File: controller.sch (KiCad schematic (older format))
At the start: 29 parts

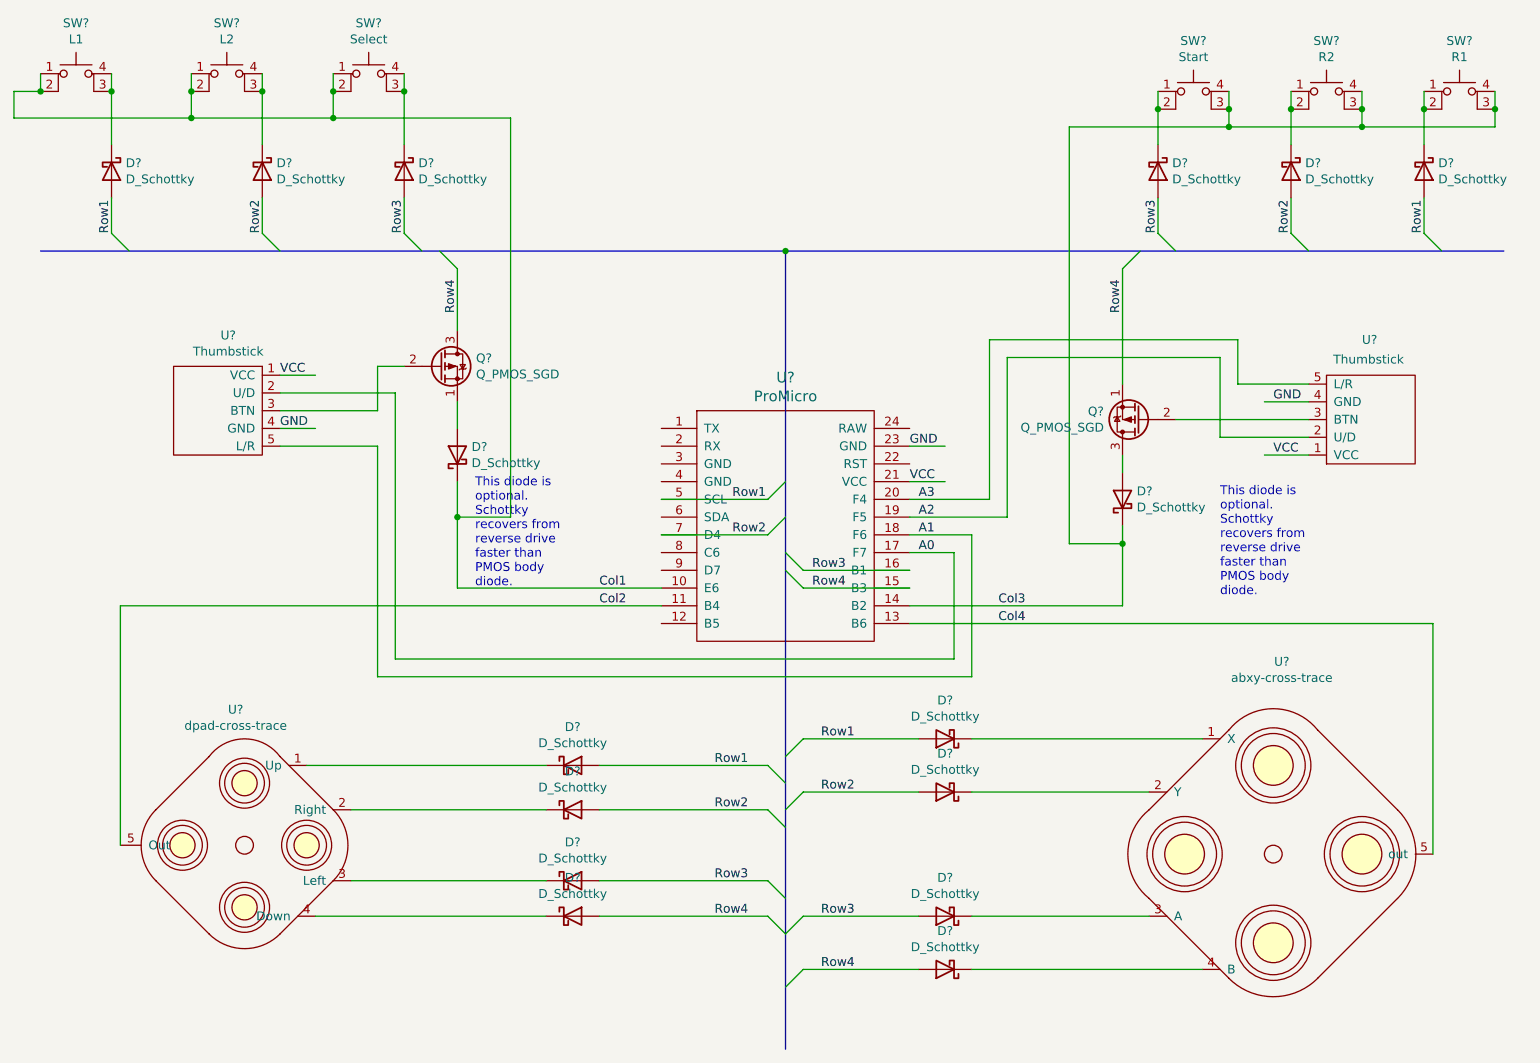
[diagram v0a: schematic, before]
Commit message: Add LM386 amp circuits and hierarchy pins.
Add two LM386 amplifier circuit schematics to audio subsystem.
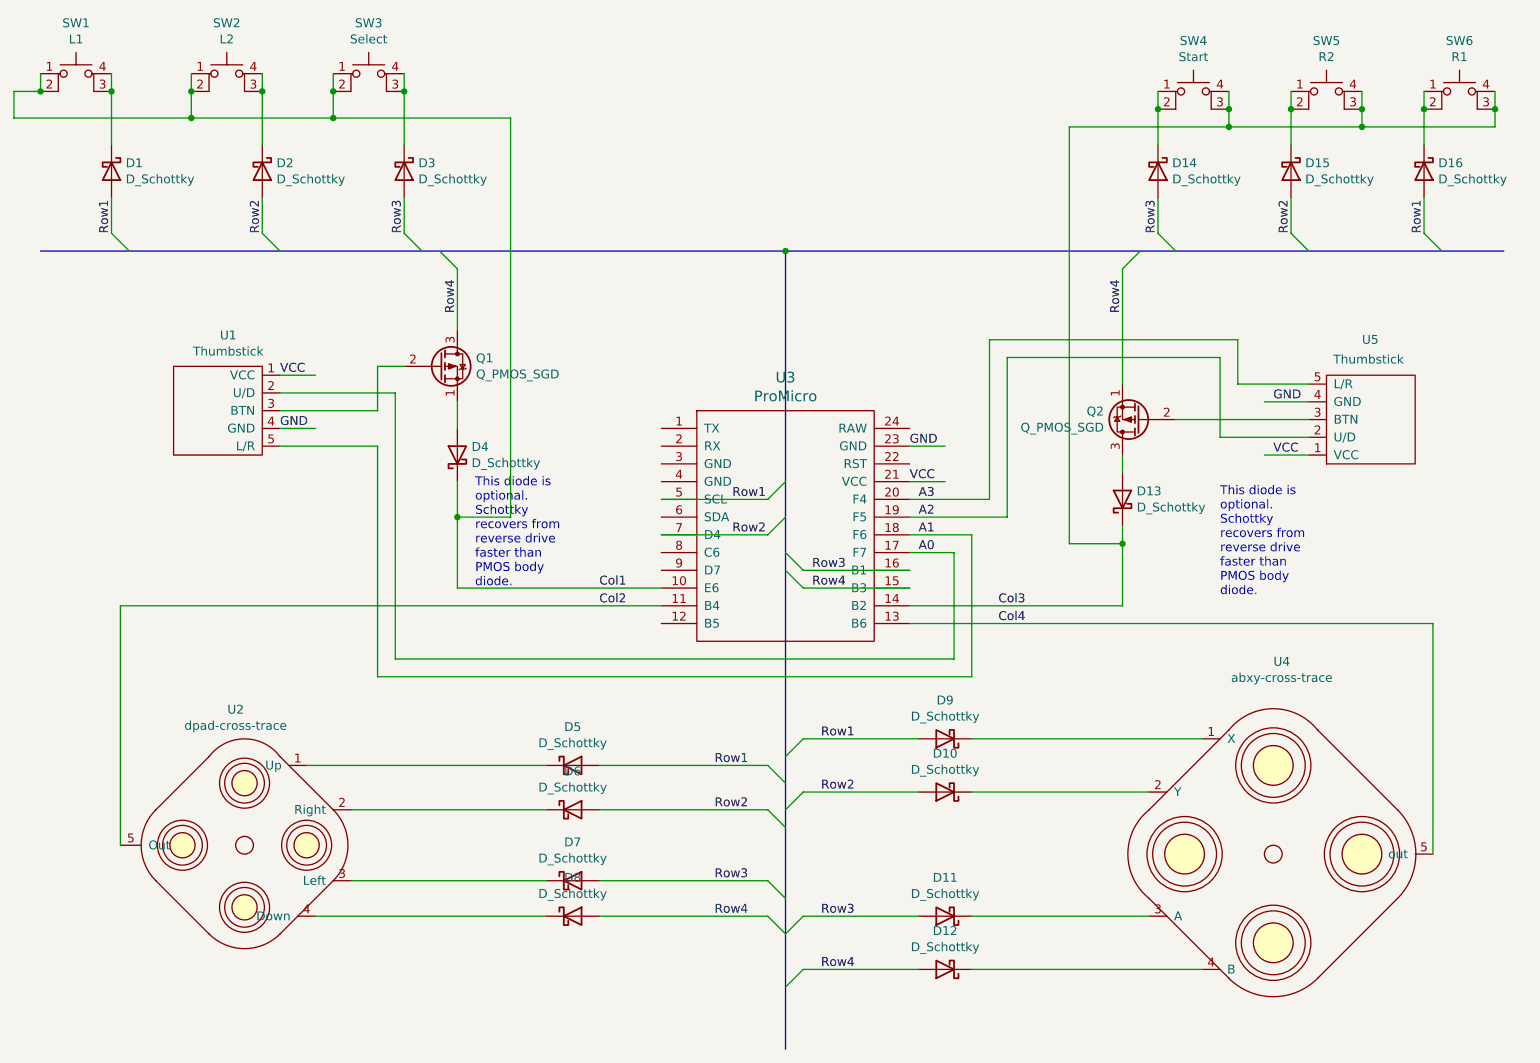
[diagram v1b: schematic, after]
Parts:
- gave numbers to parts that had none: 29
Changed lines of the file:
@@
 $EndDescr
 $Comp
-L Device:D_Schottky D?
+L Device:D_Schottky D1
 U 1 1 60680B1A
 P 2050 1650
-F 0 "D?" V 2004 1730 50  0000 L CNN
+F 0 "D1" V 2004 1730 50  0000 L CNN
 F 1 "D_Schottky" V 2095 1730 50  0000 L CNN
 F 2 "" H 2050 1650 50  0001 C CNN
@@
 $EndComp
 $Comp
-L Switch:SW_MEC_5E SW?
+L Switch:SW_MEC_5E SW1
 U 1 1 60680B20
 P 1850 1200
-F 0 "SW?" H 1850 1585 50  0000 C CNN
+F 0 "SW1" H 1850 1585 50  0000 C CNN
 F 1 "L1" H 1850 1494 50  0000 C CNN
 F 2 "" H 1850 1500 50  0001 C CNN
@@
 $EndComp
 $Comp
-L Switch:SW_MEC_5E SW?
+L Switch:SW_MEC_5E SW3
 U 1 1 60680B26
 P 3500 1200
-F 0 "SW?" H 3500 1585 50  0000 C CNN
+F 0 "SW3" H 3500 1585 50  0000 C CNN
 F 1 "Select" H 3500 1494 50  0000 C CNN
 F 2 "" H 3500 1500 50  0001 C CNN
@@
 $EndComp
 $Comp
-L Switch:SW_MEC_5E SW?
+L Switch:SW_MEC_5E SW2
 U 1 1 60680B2C
 P 2700 1200
-F 0 "SW?" H 2700 1585 50  0000 C CNN
+F 0 "SW2" H 2700 1585 50  0000 C CNN
 F 1 "L2" H 2700 1494 50  0000 C CNN
 F 2 "" H 2700 1500 50  0001 C CNN
@@
 $EndComp
 $Comp
-L Switch:SW_MEC_5E SW?
+L Switch:SW_MEC_5E SW5
 U 1 1 60680B32
 P 8900 1300
-F 0 "SW?" H 8900 1685 50  0000 C CNN
+F 0 "SW5" H 8900 1685 50  0000 C CNN
 F 1 "R2" H 8900 1594 50  0000 C CNN
 F 2 "" H 8900 1600 50  0001 C CNN
@@
 $EndComp
 $Comp
-L Switch:SW_MEC_5E SW?
+L Switch:SW_MEC_5E SW4
 U 1 1 60680B38
 P 8150 1300
-F 0 "SW?" H 8150 1685 50  0000 C CNN
+F 0 "SW4" H 8150 1685 50  0000 C CNN
 F 1 "Start" H 8150 1594 50  0000 C CNN
 F 2 "" H 8150 1600 50  0001 C CNN
@@
 $EndComp
 $Comp
-L Device:Q_PMOS_SGD Q?
+L Device:Q_PMOS_SGD Q1
 U 1 1 60680B3E
 P 3900 2750
-F 0 "Q?" H 4105 2796 50  0000 L CNN
+F 0 "Q1" H 4105 2796 50  0000 L CNN
 F 1 "Q_PMOS_SGD" H 4105 2705 50  0000 L CNN
 F 2 "" H 4100 2850 50  0001 C CNN
@@
 $EndComp
 $Comp
-L Device:Q_PMOS_SGD Q?
+L Device:Q_PMOS_SGD Q2
 U 1 1 60680B44
 P 7850 3050
-F 0 "Q?" H 8055 3004 50  0000 L CNN
+F 0 "Q2" H 8055 3004 50  0000 L CNN
 F 1 "Q_PMOS_SGD" H 8055 3095 50  0000 L CNN
 F 2 "" H 8050 3150 50  0001 C CNN
@@
 $EndComp
 $Comp
-L rpi-shell:Thumbstick U?
+L rpi-shell:Thumbstick U1
 U 1 1 60680B4A
 P 2650 3000
-F 0 "U?" H 2708 3425 50  0000 C CNN
+F 0 "U1" H 2708 3425 50  0000 C CNN
 F 1 "Thumbstick" H 2708 3334 50  0000 C CNN
 F 2 "" H 2650 3150 50  0001 C CNN
@@
 $EndComp
 $Comp
-L rpi-shell:Thumbstick U?
+L rpi-shell:Thumbstick U5
 U 1 1 60680B50
 P 9150 3050
-F 0 "U?" H 9200 2600 50  0000 R CNN
+F 0 "U5" H 9200 2600 50  0000 R CNN
 F 1 "Thumbstick" H 9362 2711 50  0000 R CNN
 F 2 "" H 9150 3200 50  0001 C CNN
@@
 	4000 4000 5150 4000
 $Comp
-L promicro:ProMicro U?
+L promicro:ProMicro U3
 U 1 1 60680B58
 P 5850 3850
-F 0 "U?" H 5850 4887 60  0000 C CNN
+F 0 "U3" H 5850 4887 60  0000 C CNN
 F 1 "ProMicro" H 5850 4781 60  0000 C CNN
 F 2 "" H 5950 2800 60  0000 C CNN
@@
 	2050 1100 2050 1200
 $Comp
-L Device:D_Schottky D?
+L Device:D_Schottky D2
 U 1 1 60680B6E
 P 2900 1650
-F 0 "D?" V 2854 1730 50  0000 L CNN
+F 0 "D2" V 2854 1730 50  0000 L CNN
 F 1 "D_Schottky" V 2945 1730 50  0000 L CNN
 F 2 "" H 2900 1650 50  0001 C CNN
@@
 $EndComp
 $Comp
-L Device:D_Schottky D?
+L Device:D_Schottky D3
 U 1 1 60680B74
 P 3700 1650
-F 0 "D?" V 3654 1730 50  0000 L CNN
+F 0 "D3" V 3654 1730 50  0000 L CNN
 F 1 "D_Schottky" V 3745 1730 50  0000 L CNN
 F 2 "" H 3700 1650 50  0001 C CNN
@@
 	4000 3600 4000 4000
 $Comp
-L Device:D_Schottky D?
+L Device:D_Schottky D14
 U 1 1 60680B83
 P 7950 1650
-F 0 "D?" V 7904 1730 50  0000 L CNN
+F 0 "D14" V 7904 1730 50  0000 L CNN
 F 1 "D_Schottky" V 7995 1730 50  0000 L CNN
 F 2 "" H 7950 1650 50  0001 C CNN
@@
 $EndComp
 $Comp
-L Device:D_Schottky D?
+L Device:D_Schottky D15
 U 1 1 60680B89
 P 8700 1650
-F 0 "D?" V 8654 1730 50  0000 L CNN
+F 0 "D15" V 8654 1730 50  0000 L CNN
 F 1 "D_Schottky" V 8745 1730 50  0000 L CNN
 F 2 "" H 8700 1650 50  0001 C CNN
@@
 $EndComp
 $Comp
-L Device:D_Schottky D?
+L Device:D_Schottky D16
 U 1 1 60680B8F
 P 9450 1650
-F 0 "D?" V 9404 1730 50  0000 L CNN
+F 0 "D16" V 9404 1730 50  0000 L CNN
 F 1 "D_Schottky" V 9495 1730 50  0000 L CNN
 F 2 "" H 9450 1650 50  0001 C CNN
@@
 	4300 3600 4000 3600
 $Comp
-L Switch:SW_MEC_5E SW?
+L Switch:SW_MEC_5E SW6
 U 1 1 60680BB6
 P 9650 1300
-F 0 "SW?" H 9650 1685 50  0000 C CNN
+F 0 "SW6" H 9650 1685 50  0000 C CNN
 F 1 "R1" H 9650 1594 50  0000 C CNN
 F 2 "" H 9650 1600 50  0001 C CNN
@@
 	3550 3000 3000 3000
 $Comp
-L Device:D_Schottky D?
+L Device:D_Schottky D4
 U 1 1 60680C01
 P 4000 3250
-F 0 "D?" V 4046 3170 50  0000 R CNN
+F 0 "D4" V 4046 3170 50  0000 R CNN
 F 1 "D_Schottky" V 3955 3170 50  0000 R CNN
 F 2 "" H 4000 3250 50  0001 C CNN
@@
 This diode is\noptional.\nSchottky\nrecovers from\nreverse drive\nfaster than \nPMOS body \ndiode.\n
 $Comp
-L Device:D_Schottky D?
+L Device:D_Schottky D13
 U 1 1 60680C0B
 P 7750 3500
-F 0 "D?" V 7796 3420 50  0000 R CNN
+F 0 "D13" V 7796 3420 50  0000 R CNN
 F 1 "D_Schottky" V 7705 3420 50  0000 R CNN
 F 2 "" H 7750 3500 50  0001 C CNN
@@
 This diode is\noptional.\nSchottky\nrecovers from\nreverse drive\nfaster than \nPMOS body \ndiode.\n
 $Comp
-L Device:D_Schottky D?
+L Device:D_Schottky D10
 U 1 1 60680C20
 P 6750 5150
-F 0 "D?" H 6750 4933 50  0000 C CNN
+F 0 "D10" H 6750 4933 50  0000 C CNN
 F 1 "D_Schottky" H 6750 5024 50  0000 C CNN
 F 2 "" H 6750 5150 50  0001 C CNN
@@
 $EndComp
 $Comp
-L Device:D_Schottky D?
+L Device:D_Schottky D11
 U 1 1 60680C26
 P 6750 5850
-F 0 "D?" H 6750 5633 50  0000 C CNN
+F 0 "D11" H 6750 5633 50  0000 C CNN
 F 1 "D_Schottky" H 6750 5724 50  0000 C CNN
 F 2 "" H 6750 5850 50  0001 C CNN
@@
 $EndComp
 $Comp
-L Device:D_Schottky D?
+L Device:D_Schottky D12
 U 1 1 60680C2C
 P 6750 6150
-F 0 "D?" H 6750 5933 50  0000 C CNN
+F 0 "D12" H 6750 5933 50  0000 C CNN
 F 1 "D_Schottky" H 6750 6024 50  0000 C CNN
 F 2 "" H 6750 6150 50  0001 C CNN
@@
 	5950 6150 6600 6150
 $Comp
-L Device:D_Schottky D?
+L Device:D_Schottky D5
 U 1 1 60680C36
 P 4650 5000
-F 0 "D?" H 4650 5217 50  0000 C CNN
+F 0 "D5" H 4650 5217 50  0000 C CNN
 F 1 "D_Schottky" H 4650 5126 50  0000 C CNN
 F 2 "" H 4650 5000 50  0001 C CNN
@@
 $EndComp
 $Comp
-L Device:D_Schottky D?
+L Device:D_Schottky D6
 U 1 1 60680C3C
 P 4650 5250
-F 0 "D?" H 4650 5467 50  0000 C CNN
+F 0 "D6" H 4650 5467 50  0000 C CNN
 F 1 "D_Schottky" H 4650 5376 50  0000 C CNN
 F 2 "" H 4650 5250 50  0001 C CNN
@@
 $EndComp
 $Comp
-L Device:D_Schottky D?
+L Device:D_Schottky D7
 U 1 1 60680C42
 P 4650 5650
-F 0 "D?" H 4650 5867 50  0000 C CNN
+F 0 "D7" H 4650 5867 50  0000 C CNN
 F 1 "D_Schottky" H 4650 5776 50  0000 C CNN
 F 2 "" H 4650 5650 50  0001 C CNN
@@
 $EndComp
 $Comp
-L Device:D_Schottky D?
+L Device:D_Schottky D8
 U 1 1 60680C48
 P 4650 5850
-F 0 "D?" H 4650 6067 50  0000 C CNN
+F 0 "D8" H 4650 6067 50  0000 C CNN
 F 1 "D_Schottky" H 4650 5976 50  0000 C CNN
 F 2 "" H 4650 5850 50  0001 C CNN
@@
 Col4
 $Comp
-L rpi-shell:dpad-cross-trace U?
+L rpi-shell:dpad-cross-trace U2
 U 1 1 60680C54
 P 2800 5450
-F 0 "U?" H 2750 6215 50  0000 C CNN
+F 0 "U2" H 2750 6215 50  0000 C CNN
 F 1 "dpad-cross-trace" H 2750 6124 50  0000 C CNN
 F 2 "" H 2800 4400 50  0001 C CNN
@@
 	2100 4100 5150 4100
 $Comp
-L Device:D_Schottky D?
+L Device:D_Schottky D9
 U 1 1 60680C64
 P 6750 4850
-F 0 "D?" H 6750 4633 50  0000 C CNN
+F 0 "D9" H 6750 4633 50  0000 C CNN
 F 1 "D_Schottky" H 6750 4724 50  0000 C CNN
 F 2 "" H 6750 4850 50  0001 C CNN
@@
 $EndComp
 $Comp
-L rpi-shell:abxy-cross-trace U?
+L rpi-shell:abxy-cross-trace U4
 U 1 1 60680C6A
 P 8600 5500
-F 0 "U?" H 8648 6585 50  0000 C CNN
+F 0 "U4" H 8648 6585 50  0000 C CNN
 F 1 "abxy-cross-trace" H 8648 6494 50  0000 C CNN
 F 2 "" H 8600 5500 50  0001 C CNN

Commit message: Fix power pins to remove ERC warnings.
Add global VCC and GND power pins. Add PWR_FLAG to Arduino VCC and to
audio subsystem power pins to remove ERC warnings.

Add Not Connected to all applicable pins.
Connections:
- no-connect marks 0 -> 10
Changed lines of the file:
@@
 VCC
 Wire Wire Line
-	6550 3400 6750 3400
+	6550 3400 6800 3400
 Wire Wire Line
 	8800 3250 8550 3250
@@
 	8800 2950 8550 2950
 Wire Wire Line
-	6550 3200 6750 3200
+	6550 3200 6800 3200
 Text Label 6550 3200 0    50   ~ 0
 GND
@@
 Text Label 6600 3500 0    50   ~ 0
 A3
+NoConn ~ 5150 3100
+NoConn ~ 5150 3200
+NoConn ~ 5150 3300
+NoConn ~ 5150 3400
+NoConn ~ 5150 3600
+NoConn ~ 5150 3800
+NoConn ~ 5150 3900
+NoConn ~ 5150 4200
+NoConn ~ 6550 3300
+NoConn ~ 6550 3100
+$Comp
+L power:PWR_FLAG #FLG0104
+U 1 1 606B0D7F
+P 6800 3400
+F 0 "#FLG0104" H 6800 3475 50  0001 C CNN
+F 1 "PWR_FLAG" H 6800 3573 50  0000 C CNN
+F 2 "" H 6800 3400 50  0001 C CNN
+F 3 "~" H 6800 3400 50  0001 C CNN
+	1    6800 3400
+	1    0    0    -1
+$EndComp
 Wire Bus Line
 	5850 2100 9900 2100
